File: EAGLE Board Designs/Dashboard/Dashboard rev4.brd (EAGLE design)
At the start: 209.1 x 43.5 mm, 109 parts, among them J1 CONNECTOR-AVR-ISP_2X05_SMD, J2 CONNECTOR-6_μF_S_RA_, J3 CONNECTOR-CAN_μF_S_RA_, J4 CONNECTOR-8_μF_S_RA_, J5 JUMPER_0603_, Q1 TRANSISTOR_N_MOS__PMV15ENEA, Q2 TRANSISTOR_N_MOS__PMV15ENEA, Q3 TRANSISTOR_N_MOS__PMV15ENEA, Q4 TRANSISTOR_N_MOS__PMV15ENEA, Q5 TRANSISTOR_N_MOS__PMV15ENEA, Q6 TRANSISTOR_N_MOS__PMV15ENEA, Q7 TRANSISTOR_N_MOS__PMV15ENEA, Q8 TRANSISTOR_N_MOS__PMV15ENEA, Q9 TRANSISTOR_N_MOS__PMV15ENEA, U1 ATMEGA328P-AU, U2 RE46C100, U3 MCP23S08, U4 MCP2562FD, U5 MCP2515, U6 LOGICGATE_INVERTER_DCK3, U7 LOGICGATE_INVERTER_DCK3, X1 CRYSTAL_16MHZ, X2 CRYSTAL_16MHZ

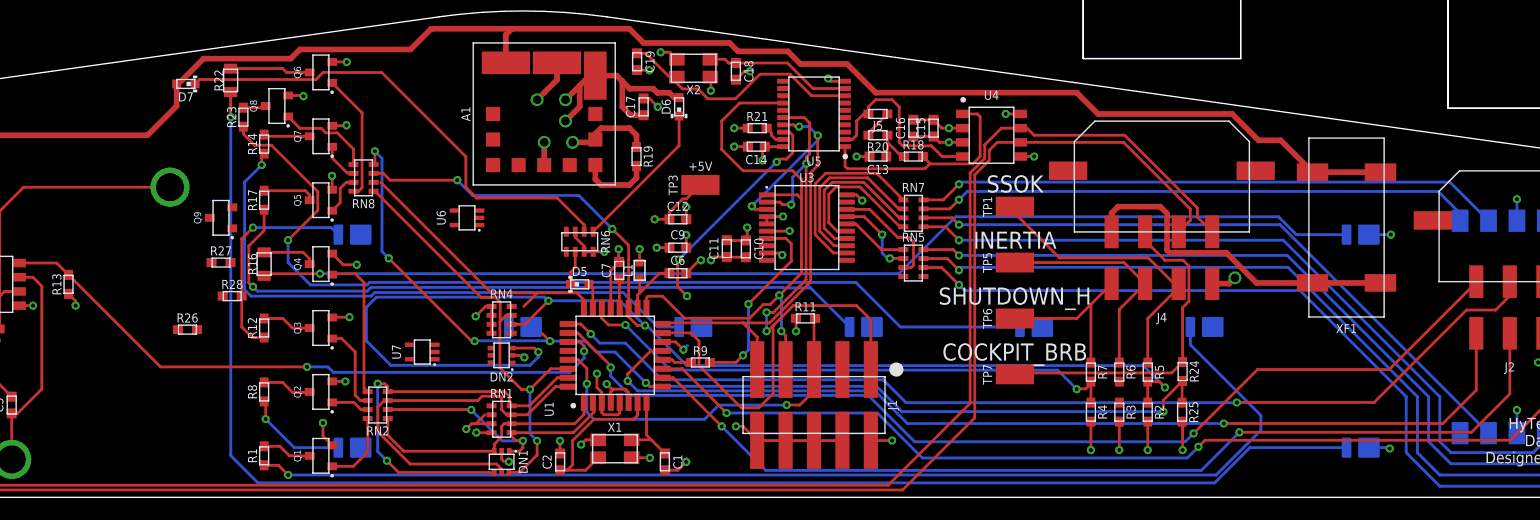
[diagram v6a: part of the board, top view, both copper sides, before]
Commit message: Finished cleaning up traces and labeling some nets
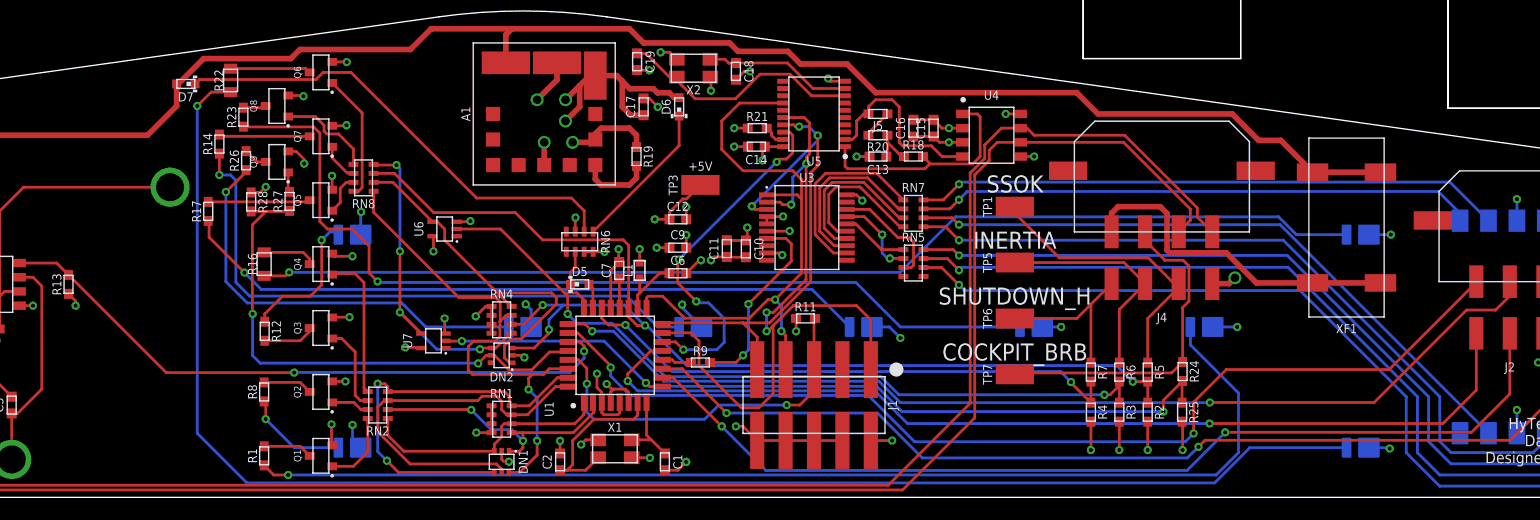
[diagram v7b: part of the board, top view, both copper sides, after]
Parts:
- moved R26 16.0 mm to (-24.8, 30.1), turned to 90 degrees
- moved R28 8.59 mm to (-24.3, 26.4), turned to 270 degrees
- moved R27 8.21 mm to (-20.9, 26.5), turned to 90 degrees
- moved Q9 7.07 mm to (-22.0, 30.0)
- moved R17 5.10 mm to (-28.1, 25.6)
- moved R14 4.00 mm to (-27.1, 31.6)
- moved U6 2.24 mm to (-7.00, 24.0)
- moved U7 1.41 mm to (-8.00, 14.0)
- moved R12 0.29 mm to (-23.1, 14.9), turned to 270 degrees
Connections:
- net N$2 renamed MCU_LED-
- net N$20 renamed BRB_LED-
- net N$24 renamed MODE_LED-
- net N$25 renamed IMD_LED-
- net N$27 renamed AMS_LED-
- net N$31 renamed START_LED-
- net N$33 renamed TRACTIVE_LED-
- net N$40 renamed S/D_G_LED-
- net N$49 renamed S/D_F_LED-
- removed net N$32: D104.A, D105.A, D8.A
- net +5V: now also D104.A, D105.A, D8.A
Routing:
- net LED_TRACTIVE: track 0.00 -> 46.9 mm, vias 0 -> 2
- net SHUTDOWN_G_READ: track 25.0 -> 71.3 mm, vias 0 -> 2
- net TRACTIVE_LED-: track 0.00 -> 37.7 mm, vias 0 -> 1
- net SHUTDOWN_F_READ: track 139.1 -> 102.9 mm, vias 6 -> 4
- net N$48: track 0.00 -> 31.7 mm
- net N$56: track 0.00 -> 30.0 mm, vias 0 -> 4
- net COCKPIT_BRB_READ: track 94.1 -> 73.8 mm, vias 6 -> 3
- net +5V: track 66.8 -> 85.8 mm, vias 20 -> 29
- net CS_CAN: track 23.1 -> 32.6 mm
- net MODE_LED-: track 19.6 -> 12.8 mm
- net LED_AMS_CTRL: track 39.5 -> 46.4 mm
- net N$9: track 4.70 -> 9.14 mm
- net AMS_LED-: track 134.6 -> 138.7 mm
- net N$55: track 4.14 -> 8.14 mm
- net GND: track 137.0 -> 140.0 mm, vias 52 -> 56
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
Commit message: "Updated labeling"
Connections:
- net COCKPIT_BRB renamed SHUTDOWN_I
- net COCKPIT_BRB_READ renamed SHUTDOWN_I_READ
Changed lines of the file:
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@@
 <wire x1="-95.3978" y1="0" x2="100" y2="0" width="0.001" layer="20" locked="yes"/>
 <wire x1="-102.60948125" y1="25.11001875" x2="-100.36861875" y2="4.46056875" width="0.001" layer="20"/>
-<text x="74.93" y="6.985" size="3.048" layer="26" rot="MR0" align="bottom-center">AMS</text>
-<text x="74.93" y="18.035" size="3.048" layer="26" rot="MR0" align="bottom-center">IMD</text>
-<text x="60.96" y="17.78" size="3.048" layer="26" rot="MR0" align="bottom-center">MCU</text>
-<text x="30.72" y="17.78" size="3.048" layer="26" rot="MR0" align="bottom-center">INERTIA</text>
-<text x="-15" y="18.78" size="3.048" layer="26" rot="MR0" align="bottom-center">MODE</text>
-<text x="-15.24" y="6.78" size="3.048" layer="26" rot="MR0" align="bottom-center">START</text>
-<text x="15.24" y="17.78" size="3.048" layer="26" rot="MR0" align="bottom-center">SSOK</text>
+<text x="74.93" y="6.985" size="3.048" layer="22" rot="MR0" align="bottom-center">AMS</text>
+<text x="74.93" y="18.035" size="3.048" layer="22" rot="MR0" align="bottom-center">IMD</text>
+<text x="60.96" y="17.78" size="3.048" layer="22" rot="MR0" align="bottom-center">MCU</text>
+<text x="30.72" y="17.78" size="3.048" layer="22" rot="MR0" align="bottom-center">INERTIA</text>
+<text x="-15" y="18.78" size="3.048" layer="22" rot="MR0" align="bottom-center">MODE</text>
+<text x="-15.24" y="6.78" size="3.048" layer="22" rot="MR0" align="bottom-center">START</text>
+<text x="15.24" y="17.78" size="3.048" layer="22" rot="MR0" align="bottom-center">SSOK</text>
 <text x="94.615" y="5.08" size="1.016" layer="21" font="vector" align="center">HyTech Racing 2022
 Dashboard rev4
@@
 <text x="44" y="22.238" size="1.524" layer="21" font="vector" align="bottom-center">INERTIA</text>
 <text x="44" y="17.238" size="1.524" layer="21" font="vector" align="bottom-center">SHUTDOWN_H</text>
-<text x="45.24" y="17.78" size="3.048" layer="26" rot="MR0" align="bottom-center">BRB</text>
+<text x="45.24" y="17.78" size="3.048" layer="22" rot="MR0" align="bottom-center">BRB</text>
 <text x="44" y="12.238" size="1.524" layer="21" font="vector" align="bottom-center">COCKPIT_BRB</text>
-<text x="0" y="17.78" size="3.048" layer="26" rot="MR0" align="bottom-center">TSB</text>
+<text x="0" y="17.78" size="3.048" layer="22" rot="MR0" align="bottom-center">TSB</text>
 </plain>
 <attributes>
@@
 <wire x1="52.65" y1="25.412" x2="52.65" y2="23.7363" width="0.508" layer="1"/>
 </signal>
-<signal name="COCKPIT_BRB">
+<signal name="SHUTDOWN_I">
 <contactref element="J4" pad="2"/>
 <contactref element="R24" pad="1"/>
@@
 <wire x1="-23.1533" y1="34.85" x2="-25" y2="34.85" width="0.254" layer="1"/>
 </signal>
-<signal name="COCKPIT_BRB_READ">
+<signal name="SHUTDOWN_I_READ">
 <contactref element="R24" pad="2"/>
 <contactref element="U1" pad="9"/>
